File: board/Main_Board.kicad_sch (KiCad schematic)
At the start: 5 parts, among them U1 Teensy4.1_DEV-16771

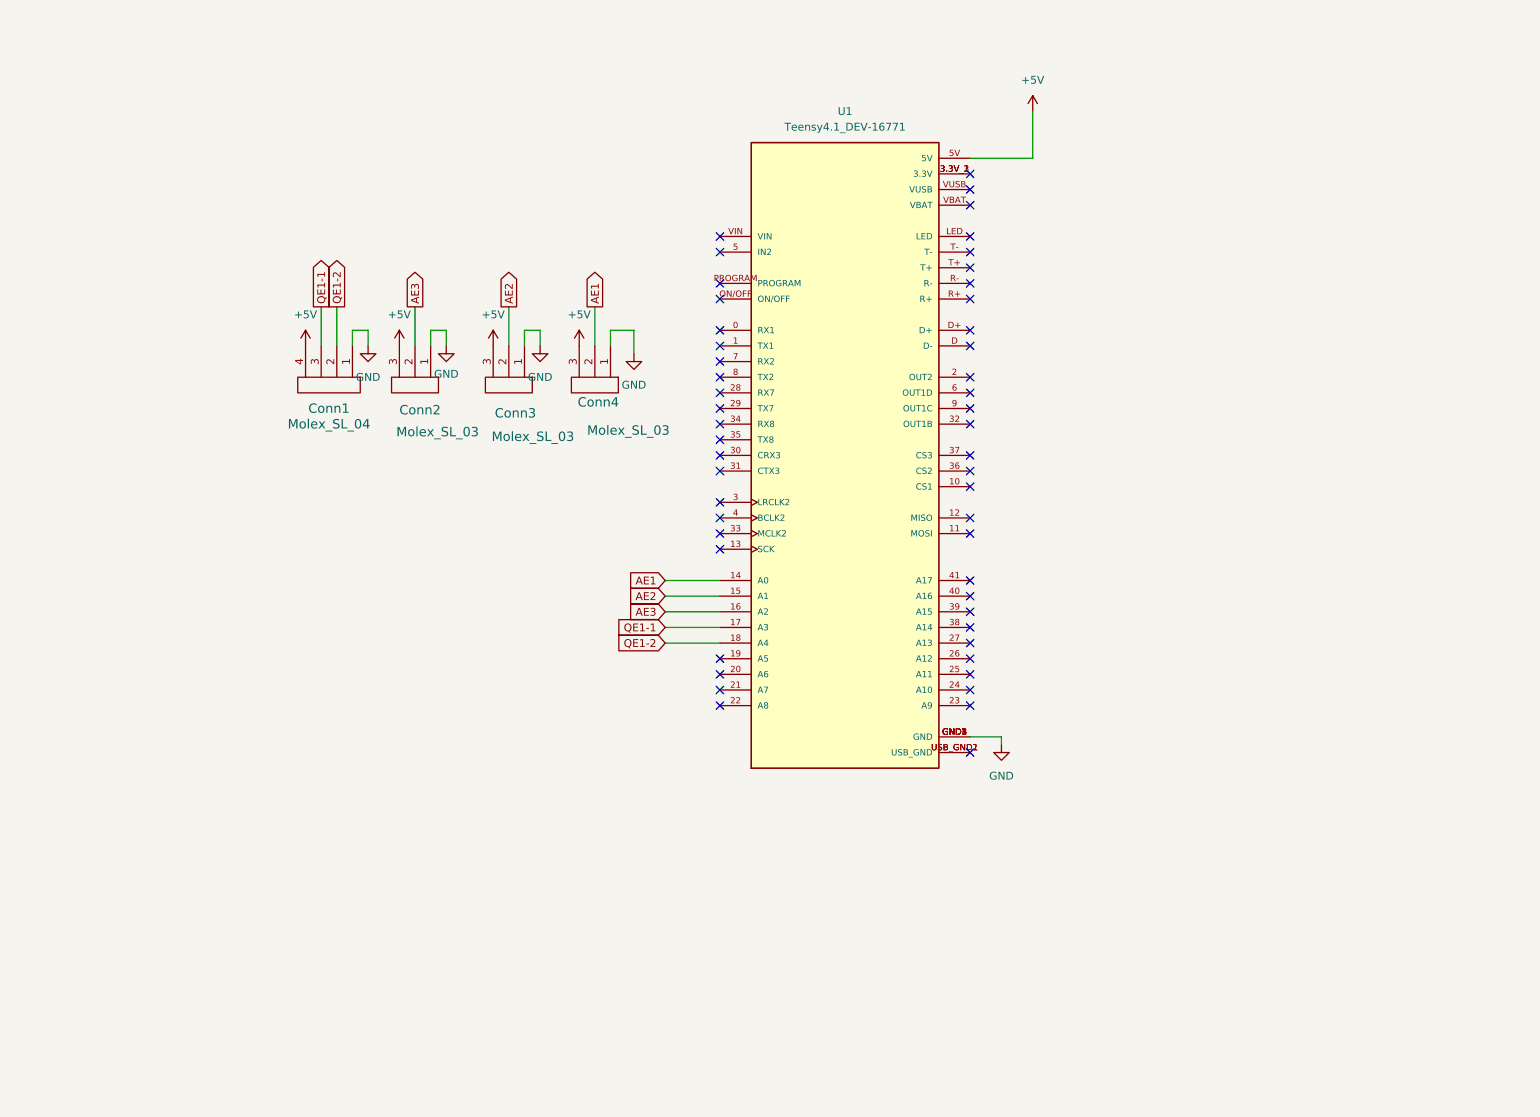
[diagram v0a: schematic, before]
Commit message: Fix Schematic after Review
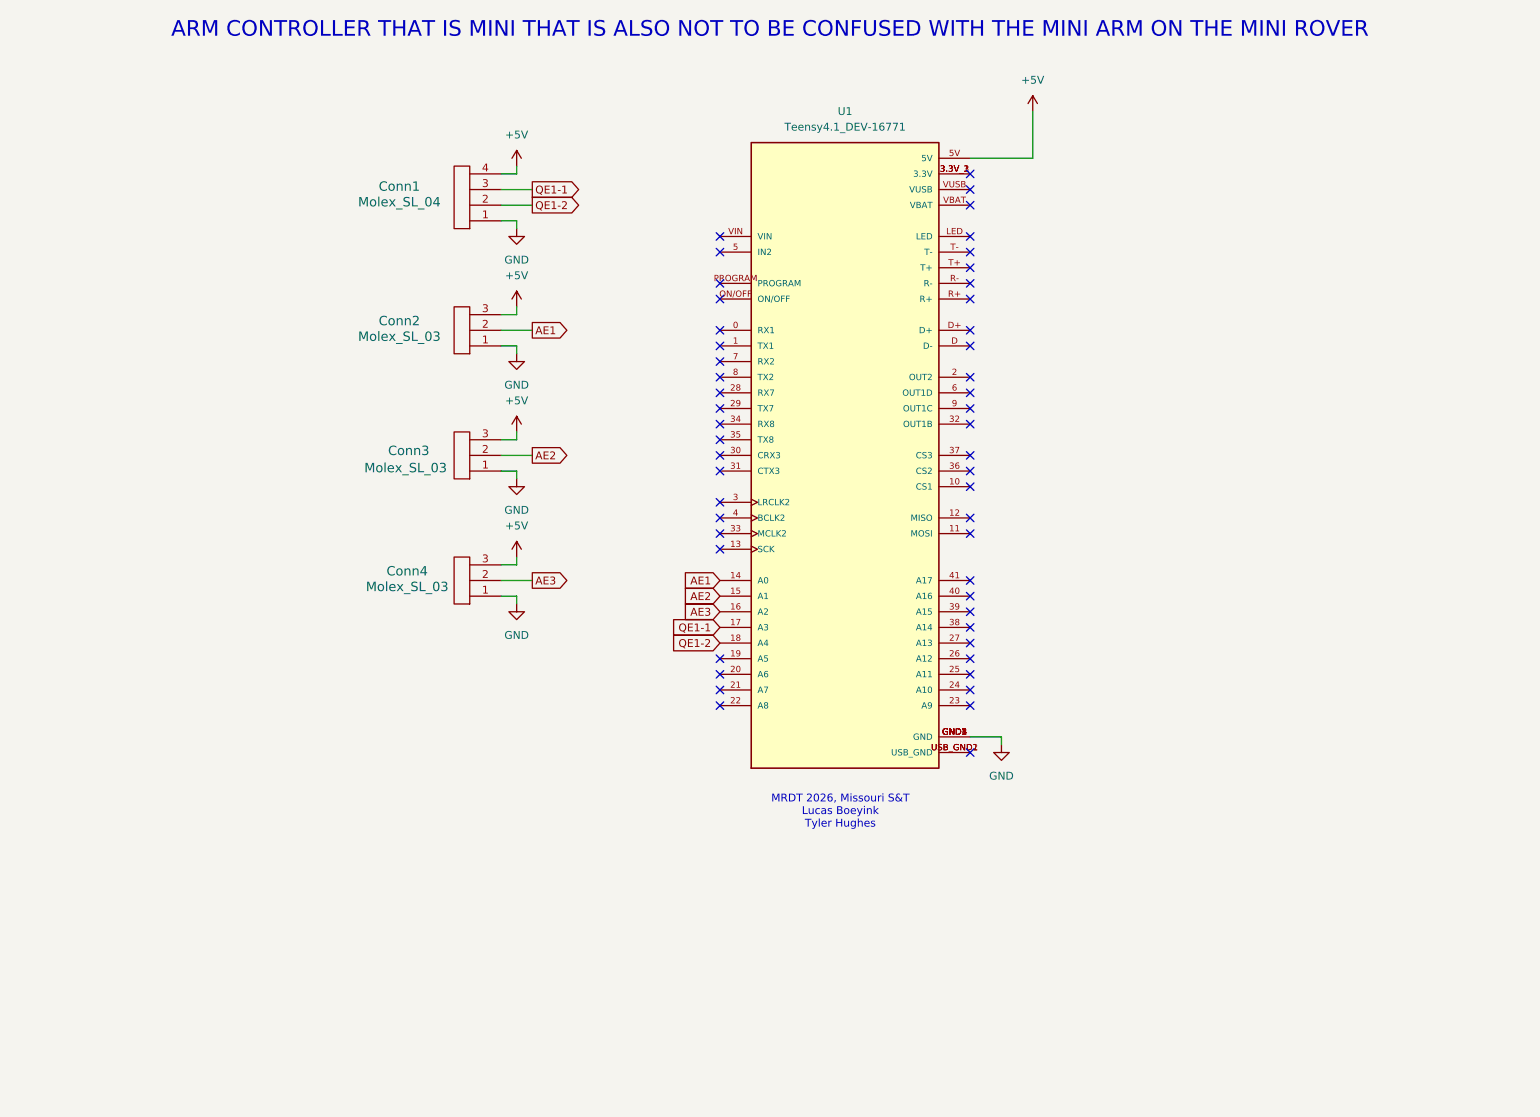
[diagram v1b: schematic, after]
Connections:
- net AE1: now also Conn2.2; no longer Conn4.2
- net AE3: now also Conn4.2; no longer Conn2.2
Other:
- note added: "ARM CONTROLLER THAT IS MINI THAT IS ALSO NOT TO BE CONFUSED WITH THE MINI ARM ON THE MINI ROVER"
- note added: "MRDT 2026, Missouri S&T Lucas Boeyink Tyler Hughes"
- moved on the sheet: Conn1

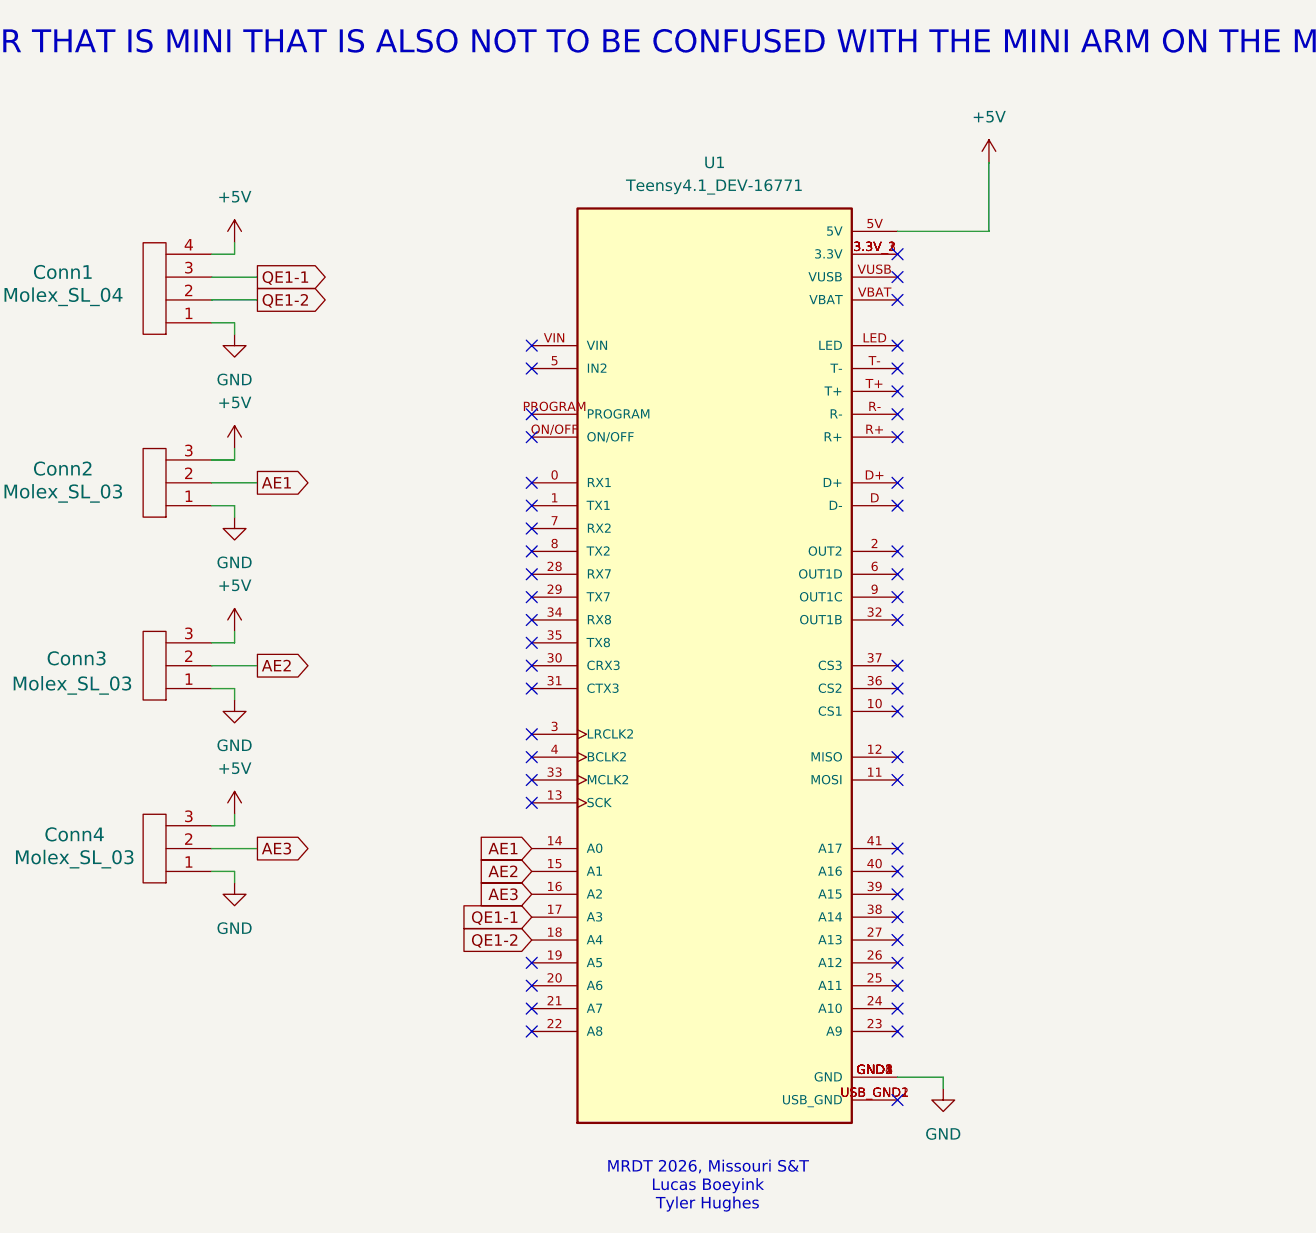
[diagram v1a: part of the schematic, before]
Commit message: Add Encoder PCB
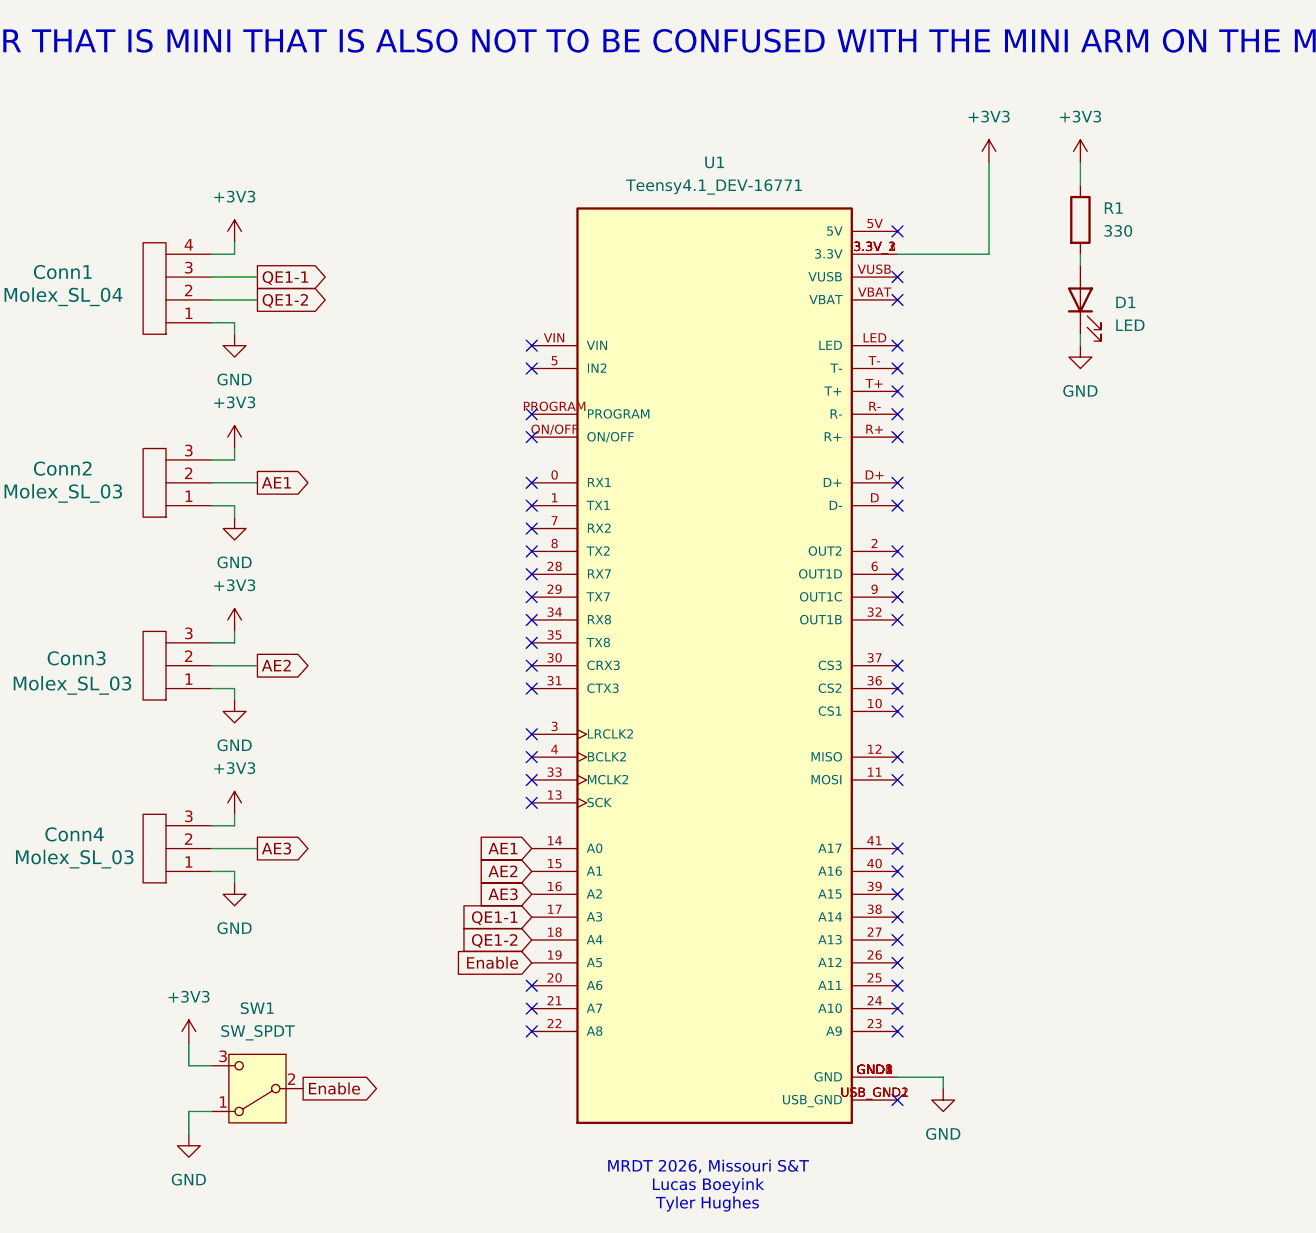
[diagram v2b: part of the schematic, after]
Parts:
- added D1: LED, LED_SMD:LED_0603_1608Metric_Pad1.05x0.95mm_HandSolder, symbol Device:LED
- added R1: 330, Resistor_SMD:R_0603_1608Metric_Pad0.98x0.95mm_HandSolder, symbol Device:R
- added SW1: SW_SPDT, Button_Switch_THT:SW_Slide_SPDT_Angled_CK_OS102011MA1Q, symbol Switch:SW_SPDT
- Conn1: footprint (none) -> Connector_JST:JST_PH_B4B-PH-K_1x04_P2.00mm_Vertical
- Conn2, Conn3, Conn4: footprint (none) -> Connector_JST:JST_PH_B3B-PH-K_1x03_P2.00mm_Vertical
- U1: footprint MODULE_DEV-16771 -> MRDT_Shields:Teensy_4_1_Bare
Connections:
- net GND: now also D1.1 (K), SW1.1 (A)
- net Enable: now reaches U1.19 (A5)
- net Enable: now also SW1.2 (B)
- net +3V3: now reaches U1.3.3V_1 (3.3V), U1.3.3V_2 (3.3V), U1.3.3V_3 (3.3V)
- net +3V3: now also Conn1.4, Conn2.3, Conn3.3, Conn4.3, R1.1, SW1.3 (C)
- removed net +5V: Conn1.4, Conn2.3, Conn3.3, Conn4.3, U1.5V
- new net: D1.2 (A), R1.2
- no-connect marks 51 -> 50

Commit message: Move Power Indicators
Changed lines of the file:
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@@
 	(wire
 		(pts
-			(xy 208.28 44.45) (xy 198.12 44.45)
+			(xy 201.93 44.45) (xy 198.12 44.45)
 		)
 		(stroke
@@
 	(wire
 		(pts
-			(xy 208.28 34.29) (xy 208.28 44.45)
+			(xy 201.93 41.91) (xy 201.93 44.45)
 		)
 		(stroke
@@
 	(symbol
 		(lib_id "power:+3V3")
-		(at 208.28 34.29 0)
+		(at 201.93 41.91 0)
 		(unit 1)
 		(exclude_from_sim no)
@@
 		(fields_autoplaced yes)
 		(property "Reference" "#PWR08"
-			(at 208.28 38.1 0)
+			(at 201.93 45.72 0)
 			(effects
 				(font
@@
 		)
 		(property "Value" "+3V3"
-			(at 208.28 29.21 0)
+			(at 201.93 36.83 0)
 			(effects
 				(font
@@
 		)
 		(property "Footprint" ""
-			(at 208.28 34.29 0)
+			(at 201.93 41.91 0)
 			(effects
 				(font
@@
 		)
 		(property "Datasheet" ""
-			(at 208.28 34.29 0)
+			(at 201.93 41.91 0)
 			(effects
 				(font
@@
 		)
 		(property "Description" "Power symbol creates a global label with name \"+3V3\""
-			(at 208.28 34.29 0)
-			(effects
-				(font
+			(at 201.93 41.91 0)
+			(effects
+				(font

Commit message: Fix Breakout Board
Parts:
- added Conn5: Molex_SL_03, Connector_JST:JST_PH_B3B-PH-K_1x03_P2.00mm_Vertical, symbol MRDT_Connectors:Molex_SL_03
- added D2, D3: BLUE, symbol Device:LED
- added R2, R3: 200, symbol Device:R
- D1: value LED -> GREEN
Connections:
- net +3V3: now also Conn5.3
- net Enable: now also U1.20 (A6), D2.1 (K); no longer SW1.2 (B), U1.19 (A5)
- net GND: now also Conn5.1
- net QE1-1 renamed AE4
- net AE4: now also Conn5.2; no longer Conn1.3
- net QE1-2 renamed QE1-A
- net QE1-A: now also Conn1.3; no longer Conn1.2
- new net: D2.2 (A), R2.2
- new net: R2.1, SW1.2 (B)
- new net QE1-B: Conn1.2, U1.19 (A5)
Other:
- moved on the sheet: SW1

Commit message: Update Mini Arm Board
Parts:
- removed D2: BLUE, symbol Device:LED
- removed R2: 200, symbol Device:R
- D3: footprint (none) -> LED_SMD:LED_0603_1608Metric_Pad1.05x0.95mm_HandSolder
- R3: footprint (none) -> Resistor_SMD:R_0603_1608Metric_Pad0.98x0.95mm_HandSolder
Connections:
- net Enable: now also R3.2, SW1.2 (B)
- net GND: now also D3.1 (K)
- net at D3.2 (A): now also R3.1
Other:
- moved on the sheet: D3, SW1

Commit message: Update Main Board
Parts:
- added H1, H2, H4: MountingHole, symbol Mechanical:MountingHole
- added H3: MountingHole, MountingHole:MountingHole_4.3mm_M4_ISO14580_Pad_TopBottom, symbol Mechanical:MountingHole
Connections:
- no-connect marks 50 -> 49
